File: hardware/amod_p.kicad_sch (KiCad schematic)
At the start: 150 parts, among them J1001 SMA, J1002 SMA, J101 SMA, J102 SMA, J1101 SMA, J1102 SMA, J1103 SMA, J1104 SMA, J1105 SMA, J1201 SMA, J1301 SMA, J1302 coil, J201 SMA, J202 SMA, J301 SMA, J302 SMA, J401 SMA, J402 SMA, J501 SMA, J502 SMA, J601 SMA, J602 SMA, J701 SMA, J702 SMA, J801 SMA, J802 SMA, J901 SMA, J902 SMA, SW1201 DIP4, SW1301 DIP4, SW401 DIP2, Y801 4 MHz, Y901 455 kHz

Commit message: Silkscreen says what each tile is and whose jack is whose: jack names on their own tile's frame, titles in words on the top frame, ranges and levels placed inside; tutorial section numbers off the boards; README tables of every tile (what, chip link, specs, limits, experiments, use, what to buy) and handbook entries as tables with a picture of each tile, both from boards/tile_docs.py
Co-Authored-By: Claude Opus 5.5 <noreply@anthropic.com>
Claude-Session: https://claude.ai/code/session_01RKeoKvFFzjk3cEBLCXXHnB
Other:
- note added: "(the exact values: 2.57 uH, 269 pF, 337 nH, 2.05 nF). The tutorial's filtered chips in copper; it cleans a transmitter's"
- note added: "0.40 MHz with 470 pF; combine positions for the steps between. Into A4's LNA and the tutorial's AM radio gateware: a real station."
- note added: "1 k in series, then a 1N4148W each way to ground: whatever goes in, OUT stays within a diode drop. Harmonics: the"
- note added: "50 ohm on OUT and nothing comes back (the quarter-wave and reflection experiments). The taps are a channel's echo and a"
- note added: "A pi attenuator: 61.9 / 249 / 61.9 ohm is -20.0 dB and 50.0 ohm in a 50 ohm system (the tutorial's $10 SMA pad, on the board)."
- note added: "Before the ADC it removes the alias (the ghost image above Nyquist); after the DAC it smooths the steps."
- note added: "EXPECT: the digital-communications pages' band (a 6.25 MHz carrier): a peak at 6.3 MHz, 3 dB from 4.7 to 7.5 MHz"
- note added: "LED output or a bench supply: the knee voltage of each colour against c / lambda gives Planck's constant."
- note added: "Turns a one-bit (delta-sigma) DAC stream into a tone; a slow plant for feedback control, with P2."
- note added: "down toward f_s and leaves f_s alone: the pulling the tutorial measures against a reference. Model: C_m 15 fF, Q 50 000, C_0 4 pF (typical HC-49S)."
- note added: "harmonics and is a radio link's receiver front end."
- note added: "load would make a 1 k / 50 divider of it. The lag plant of the tutorial's feedback-control pages; the step response is 1 - exp(-t / 1 us)."
- note added: "radar target on a cable; near 16 MHz the phase velocity falls and a chirp spreads (below that, a pure-delay plant for control). A tap through 470 ohm: x1 into a"
- note added: "the peak; a resonant plant for feedback control, a lockbox's cavity before the real one. No OUT loop (the switch took its corner)."
- note added: "tutorial A quarter-wave stub, The channel, Chirps, Zadoff-Chu and LoRa, Control at the speed of the cable"
- note added: "tutorial An AM radio"
- note added: "tutorial Chirps, Zadoff-Chu and LoRa, A radio link, On the air"
- note added: "tutorial Fast captures, Chirps, Zadoff-Chu and LoRa, RC and LC circuits"
- note added: "tutorial Harmonics: a diode clipper"
- note added: "tutorial More ideas for one board"
- note added: "tutorial On the air, The modem against noise"
- note added: "tutorial RC and LC circuits"
- note added: "tutorial RC and LC circuits, Control at the speed of the cable"
- note added: "tutorial RC and LC circuits, Feedback control of an RC plant, Control at the speed of the cable"
- note added: "tutorial RC and LC circuits, The Q of a quartz crystal"
- note added: "tutorial The Q of a quartz crystal, Your crystal against a reference, More ideas for one board"
- note added: "tutorial Trading speed for bits, RC and LC circuits"
- note removed: "(the exact values: 2.57 uH, 269 pF, 337 nH, 2.05 nF). 6.10's filtered chips in copper; the transmitter's harmonics and the"
- note removed: "0.40 MHz with 470 pF; combine positions for the steps between. Into A4's LNA and 1.10's AM radio: a real station."
- note removed: "1 k in series, then a 1N4148W each way to ground: whatever goes in, OUT stays within a diode drop. 4.04's harmonics: the"
- note removed: "50 ohm on OUT and nothing comes back (4.05). The taps are 6.05's echo and 6.10's radar target; near 16 MHz the"
- note removed: "A pi attenuator: 61.9 / 249 / 61.9 ohm is -20.0 dB and 50.0 ohm in a 50 ohm system (6.12's $10 pad, on the board)."
- note removed: "Before the ADC it removes 6.10's ghost; after the DAC it smooths the steps."
- note removed: "EXPECT: Chapter 6's band: a peak at 6.3 MHz, 3 dB from 4.7 to 7.5 MHz"
- note removed: "LED output or a bench supply: the knee voltage of each colour against c / lambda gives Planck's constant (4.10)."
- note removed: "Turns 7.05's one-bit stream into a tone; the slow plant of 7.06 with P2."
- note removed: "down toward f_s and leaves f_s alone: the pulling that 4.09 measures. Model: C_m 15 fF, Q 50 000, C_0 4 pF (typical HC-49S)."
- note removed: "load would make a 1 k / 50 divider of it. The lag plant of 4.08 and 7.06; the step response is 1 - exp(-t / 1 us)."
- note removed: "phase velocity falls and a chirp spreads (7.06's pure-delay plant below that). A tap through 470 ohm: x1 into a"
- note removed: "receiver's front end of 5.07 and 6.12."
- note removed: "the peak; a resonant plant for 7.06, a lockbox's cavity before the real one. No OUT loop (the switch took its corner)."
- note removed: "tutorial 1.06, 6.10, 4.02"
- note removed: "tutorial 1.10"
- note removed: "tutorial 4.02"
- note removed: "tutorial 4.02, 4.03"
- note removed: "tutorial 4.02, 4.08, 7.06"
- note removed: "tutorial 4.02, 7.06"
- note removed: "tutorial 4.03, 4.09, 4.10"
- note removed: "tutorial 4.04"
- note removed: "tutorial 4.05, 6.05, 6.10, 7.06"
- note removed: "tutorial 4.10"
- note removed: "tutorial 6.10, 5.07, 6.12"
- note removed: "tutorial 6.12, 5.06"
- note removed: "tutorial 7.05, 4.02"

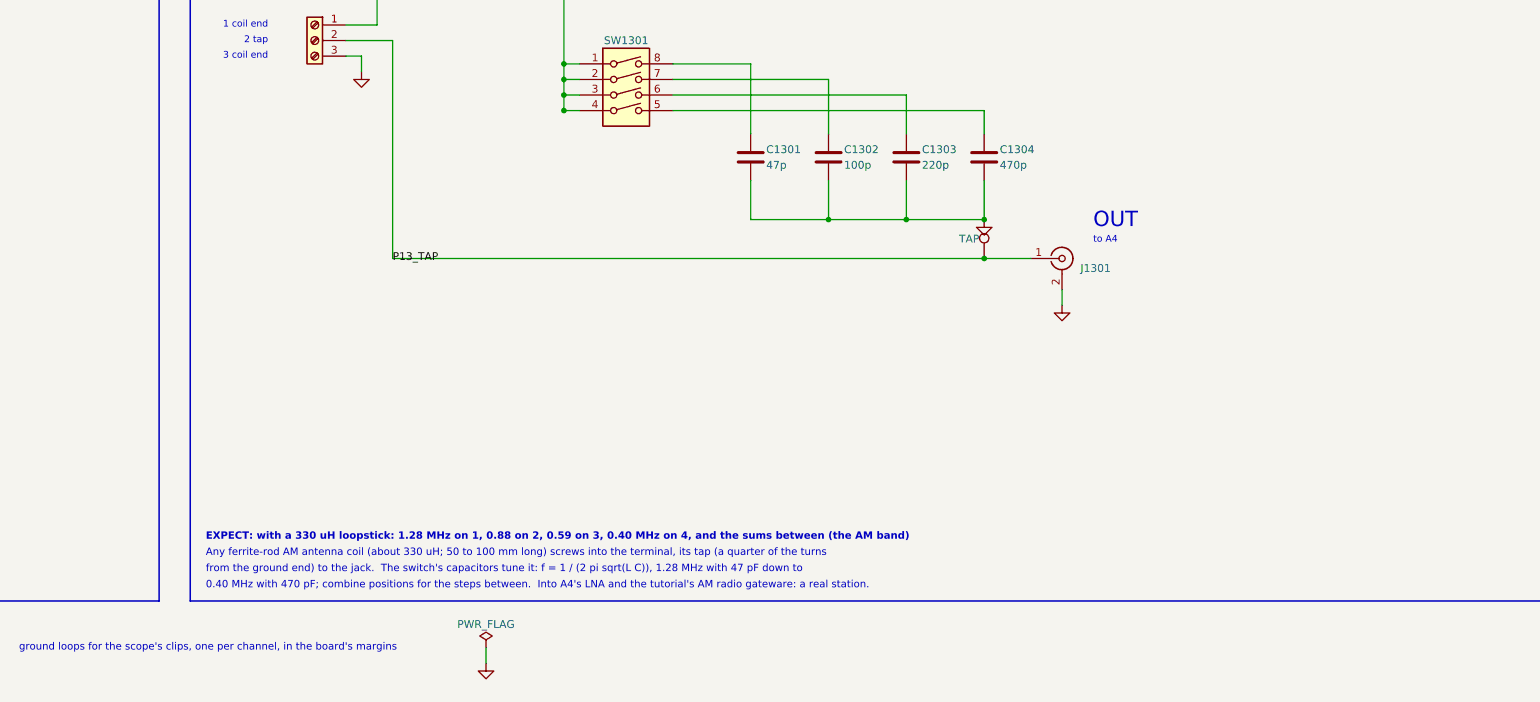
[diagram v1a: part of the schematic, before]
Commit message: P13: a VAR C screw terminal beside the coil's for an external tuning capacitor (a polyvaricon and its dial do not fit a cell); the DIP and its capacitors moved up into the right cell's top half; KIT.md lists a 365 pF air variable
Co-Authored-By: Claude Opus 5.5 <noreply@anthropic.com>
Claude-Session: https://claude.ai/code/session_01RKeoKvFFzjk3cEBLCXXHnB
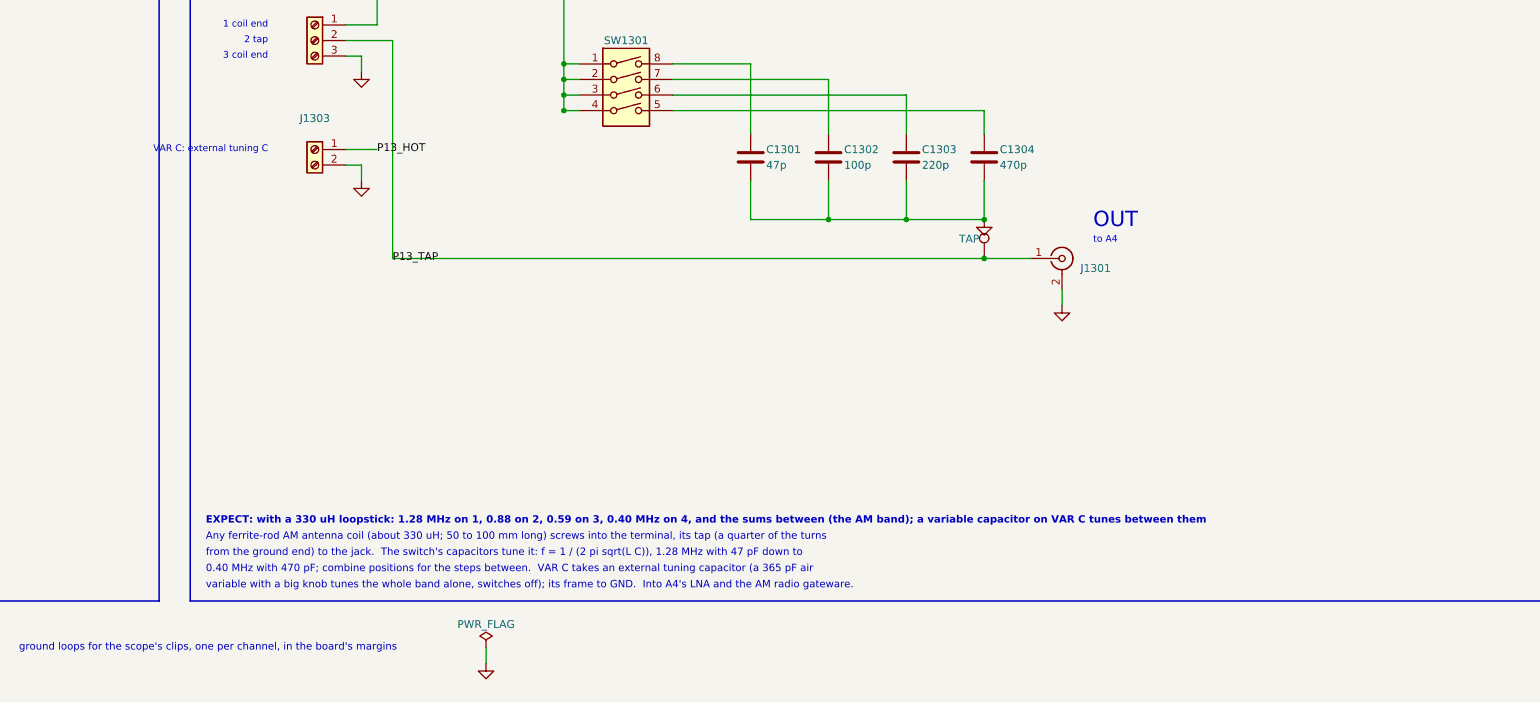
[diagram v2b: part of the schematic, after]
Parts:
- added J1303: VAR C, amod:TerminalBlock_KF301_1x02_P5.00mm, symbol Connector:Screw_Terminal_01x02
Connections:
- net GND: now also J1303.2 (Pin_2)
- net P13_HOT: now also J1303.1 (Pin_1)
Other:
- note added: "0.40 MHz with 470 pF; combine positions for the steps between. VAR C takes an external tuning capacitor (a 365 pF air"
- note added: "EXPECT: with a 330 uH loopstick: 1.28 MHz on 1, 0.88 on 2, 0.59 on 3, 0.40 MHz on 4, and the sums between (the AM band); a variable capacitor on VAR C tunes between them"
- note added: "VAR C: external tuning C"
- note added: "variable with a big knob tunes the whole band alone, switches off); its frame to GND. Into A4's LNA and the AM radio gateware."
- note removed: "0.40 MHz with 470 pF; combine positions for the steps between. Into A4's LNA and the tutorial's AM radio gateware: a real station."
- note removed: "EXPECT: with a 330 uH loopstick: 1.28 MHz on 1, 0.88 on 2, 0.59 on 3, 0.40 MHz on 4, and the sums between (the AM band)"
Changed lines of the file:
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@@
 		)
 	)
-	(text "EXPECT: with a 330 uH loopstick: 1.28 MHz on 1, 0.88 on 2, 0.59 on 3, 0.40 MHz on 4, and the sums between (the AM band)"
-		(exclude_from_sim no)
-		(at 218.44 522.94 0)
-		(effects
-			(font
-				(size 1.2 1.2)
-				(bold yes)
-			)
-			(justify left)
-		)
-	)
 	(text "P3   RC high-pass, 159 kHz"
 		(exclude_from_sim no)
@@
 		)
 	)
+	(text "EXPECT: with a 330 uH loopstick: 1.28 MHz on 1, 0.88 on 2, 0.59 on 3, 0.40 MHz on 4, and the sums between (the AM band); a variable capacitor on VAR C tunes between them"
+		(exclude_from_sim no)
+		(at 218.44 520.3 0)
+		(effects
+			(font
+				(size 1.2 1.2)
+				(bold yes)
+			)
+			(justify left)
+		)
+	)
 	(text "cell (0,2)"
 		(exclude_from_sim no)
@@
 		)
 	)
-	(text "Any ferrite-rod AM antenna coil (about 330 uH; 50 to 100 mm long) screws into the terminal, its tap (a quarter of the turns"
-		(exclude_from_sim no)
-		(at 218.44 525.58 0)
-		(effects
-			(font
-				(size 1.2 1.2)
-			)
-			(justify left)
-		)
-	)
 	(text "OUT"
 		(exclude_from_sim no)
@@
 		)
 	)
-	(text "0.40 MHz with 470 pF; combine positions for the steps between.  Into A4's LNA and the tutorial's AM radio gateware: a real station."
+	(text "Any ferrite-rod AM antenna coil (about 330 uH; 50 to 100 mm long) screws into the terminal, its tap (a quarter of the turns"
 		(exclude_from_sim no)
-		(at 218.44 530.86 0)
+		(at 218.44 522.94 0)
 		(effects
 			(font
@@
 		)
 	)
+	(text "from the ground end) to the jack.  The switch's capacitors tune it: f = 1 / (2 pi sqrt(L C)), 1.28 MHz with 47 pF down to"
+		(exclude_from_sim no)
+		(at 218.44 525.58 0)
+		(effects
+			(font
+				(size 1.2 1.2)
+			)
+			(justify left)
+		)
+	)
+	(text "VAR C: external tuning C"
+		(exclude_from_sim no)
+		(at 228.6 459.74 0)
+		(effects
+			(font
+				(size 1.1 1.1)
+			)
+			(justify right)
+		)
+	)
 	(text "IN"
 		(exclude_from_sim no)
@@
 		)
 	)
+	(text "0.40 MHz with 470 pF; combine positions for the steps between.  VAR C takes an external tuning capacitor (a 365 pF air"
+		(exclude_from_sim no)
+		(at 218.44 528.22 0)
+		(effects
+			(font
+				(size 1.2 1.2)
+			)
+			(justify left)
+		)
+	)
 	(text "tutorial RC and LC circuits, Control at the speed of the cable"
 		(exclude_from_sim no)
@@
 		)
 	)
+	(text "variable with a big knob tunes the whole band alone, switches off); its frame to GND.  Into A4's LNA and the AM radio gateware."
+		(exclude_from_sim no)
+		(at 218.44 530.86 0)
+		(effects
+			(font
+				(size 1.2 1.2)
+			)
+			(justify left)
+		)
+	)
 	(text "IN"
 		(exclude_from_sim no)
@@
 		)
 	)
-	(text "from the ground end) to the jack.  The switch's capacitors tune it: f = 1 / (2 pi sqrt(L C)), 1.28 MHz with 47 pF down to"
-		(exclude_from_sim no)
-		(at 218.44 528.22 0)
-		(effects
-			(font
-				(size 1.2 1.2)
-			)
-			(justify left)
-		)
-	)
 	(junction
 		(at 255.27 60.96)
@@
 	(wire
 		(pts
+			(xy 243.84 462.28) (xy 243.84 464.82)
+		)
+		(stroke
+			(width 0)
+			(type default)
+		)
+	)
+	(wire
+		(pts
 			(xy 231.14 335.28) (xy 233.68 335.28)
 		)
@@
 	(wire
 		(pts
+			(xy 241.3 459.74) (xy 246.38 459.74)
+		)
+		(stroke
+			(width 0)
+			(type default)
+		)
+	)
+	(wire
+		(pts
 			(xy 419.1 193.04) (xy 419.1 195.58)
 		)
@@
 	(wire
 		(pts
+			(xy 241.3 462.28) (xy 243.84 462.28)
+		)
+		(stroke
+			(width 0)
+			(type default)
+		)
+	)
+	(wire
+		(pts
 			(xy 292.1 309.88) (xy 293.37 309.88)
 		)
@@
 		)
 	)
+	(label "P13_HOT"
+		(at 246.38 459.74 0)
+		(effects
+			(font
+				(size 1.27 1.27)
+			)
+			(justify left)
+		)
+	)
 	(label "P4_IN"
 		(at 619.76 60.96 0)
@@
 	)
 	(symbol
+		(lib_id "Connector:Screw_Terminal_01x02")
+		(at 236.22 459.74 0)
+		(mirror y)
+		(unit 1)
+		(body_style 1)
+		(exclude_from_sim no)
+		(in_bom yes)
+		(on_board yes)
+		(in_pos_files yes)
+		(dnp no)
+		(property "Reference" "J1303"
+			(at 236.22 454.66 0)
+			(show_name no)
+			(do_not_autoplace no)
+			(effects
+				(font
+					(size 1.27 1.27)
+				)
+			)
+		)
+		(property "Value" "VAR C"
+			(at 236.22 464.82 0)
+			(hide yes)
+			(show_name no)
+			(do_not_autoplace no)
+			(effects
+				(font
+					(size 1.27 1.27)
+				)
+			)
+		)
+		(property "Footprint" "amod:TerminalBlock_KF301_1x02_P5.00mm"
+			(at 236.22 459.74 0)
+			(hide yes)
+			(show_name no)
+			(do_not_autoplace no)
+			(effects
+				(font
+					(size 1.27 1.27)
+				)
+			)
+		)
+		(property "Datasheet" ""
+			(at 236.22 459.74 0)
+			(hide yes)
+			(show_name no)
+			(do_not_autoplace no)
+			(effects
+				(font
+					(size 1.27 1.27)
+				)
+			)
+		)
+		(property "Description" ""
+			(at 236.22 459.74 0)
+			(hide yes)
+			(show_name no)
+			(do_not_autoplace no)
+			(effects
+				(font
+					(size 1.27 1.27)
+				)
+			)
+		)
+		(property "LCSC" "C474881"
+			(at 236.22 459.74 0)
+			(hide yes)
+			(show_name no)
+			(do_not_autoplace no)
+			(effects
+				(font
+					(size 1.27 1.27)
+				)
+			)
+		)
+		(property "MPN" "KF301-5.0-2P"
+			(at 236.22 459.74 0)
+			(hide yes)
+			(show_name no)
+			(do_not_autoplace no)
+			(effects
+				(font
+					(size 1.27 1.27)
+				)
+			)
+		)
+		(pin "1"
+		)
+		(pin "2"
+		)
+		(instances
+			(project "amod_p"
+				(path "/9eb78eaa-30d0-5848-9a54-3294ec10adc7"
+					(reference "J1303")
+					(unit 1)
+				)
+			)
+		)
+	)
+	(symbol
 		(lib_id "Connector:Conn_Coaxial")
 		(at 76.2 60.96 0)
@@
 	)
 	(symbol
+		(lib_id "power:GND")
+		(at 358.14 485.14 0)
+		(unit 1)
+		(body_style 1)
+		(exclude_from_sim no)
+		(in_bom no)
+		(on_board no)
+		(in_pos_files yes)
+		(dnp no)
+		(property "Reference" "#PWR13004"
+			(at 358.14 477.52 0)
+			(hide yes)
+			(show_name no)
+			(do_not_autoplace no)
+			(effects
+				(font
+					(size 1.27 1.27)
+				)
+			)
+		)
+		(property "Value" "GND"
+			(at 358.14 492.76 0)
+			(hide yes)
+			(show_name no)
+			(do_not_autoplace no)
+			(effects
+				(font
+					(size 1.27 1.27)
+				)
+			)
+		)
+		(property "Footprint" ""
+			(at 358.14 485.14 0)
+			(hide yes)
+			(show_name no)
+			(do_not_autoplace no)
+			(effects
+				(font
+					(size 1.27 1.27)
+				)
+			)
+		)
+		(property "Datasheet" ""
+			(at 358.14 485.14 0)
+			(hide yes)
+			(show_name no)
+			(do_not_autoplace no)
+			(effects
+				(font
+					(size 1.27 1.27)
+				)
+			)
+		)
+		(property "Description" ""
+			(at 358.14 485.14 0)
+			(hide yes)
+			(show_name no)
+			(do_not_autoplace no)
+			(effects
+				(font
+					(size 1.27 1.27)
+				)
+			)
+		)
+		(pin "1"
+		)
+		(instances
+			(project "amod_p"
+				(path "/9eb78eaa-30d0-5848-9a54-3294ec10adc7"
+					(reference "#PWR13004")
+					(unit 1)
+				)
+			)
+		)
+	)
+	(symbol
 		(lib_id "Device:C")
 		(at 293.37 316.23 0)
@@
 	(symbol
 		(lib_id "power:GND")
-		(at 358.14 485.14 0)
+		(at 243.84 464.82 0)
 		(unit 1)
 		(body_style 1)
@@
 		(dnp no)
 		(property "Reference" "#PWR13003"
-			(at 358.14 477.52 0)
+			(at 243.84 457.2 0)
 			(hide yes)
 			(show_name no)
@@
 		)
 		(property "Value" "GND"
-			(at 358.14 492.76 0)
+			(at 243.84 472.44 0)
 			(hide yes)
 			(show_name no)
@@
 		)
 		(property "Footprint" ""
-			(at 358.14 485.14 0)
+			(at 243.84 464.82 0)
 			(hide yes)
 			(show_name no)
@@
 		)
 		(property "Datasheet" ""
-			(at 358.14 485.14 0)
+			(at 243.84 464.82 0)
 			(hide yes)
 			(show_name no)
@@
 		)
 		(property "Description" ""
-			(at 358.14 485.14 0)
+			(at 243.84 464.82 0)
 			(hide yes)
 			(show_name no)
